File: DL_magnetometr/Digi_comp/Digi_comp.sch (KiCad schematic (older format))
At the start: 43 parts, among them J1 USB_B_Micro, U1 AP7331-WG-7, U2 74AHCT1G125, U3 JST-PHR-2, U4 AZ4558CM, U5 AZ4558CM, U6 AP7331-WG-7, U7 NUP2202, U8 HC-06

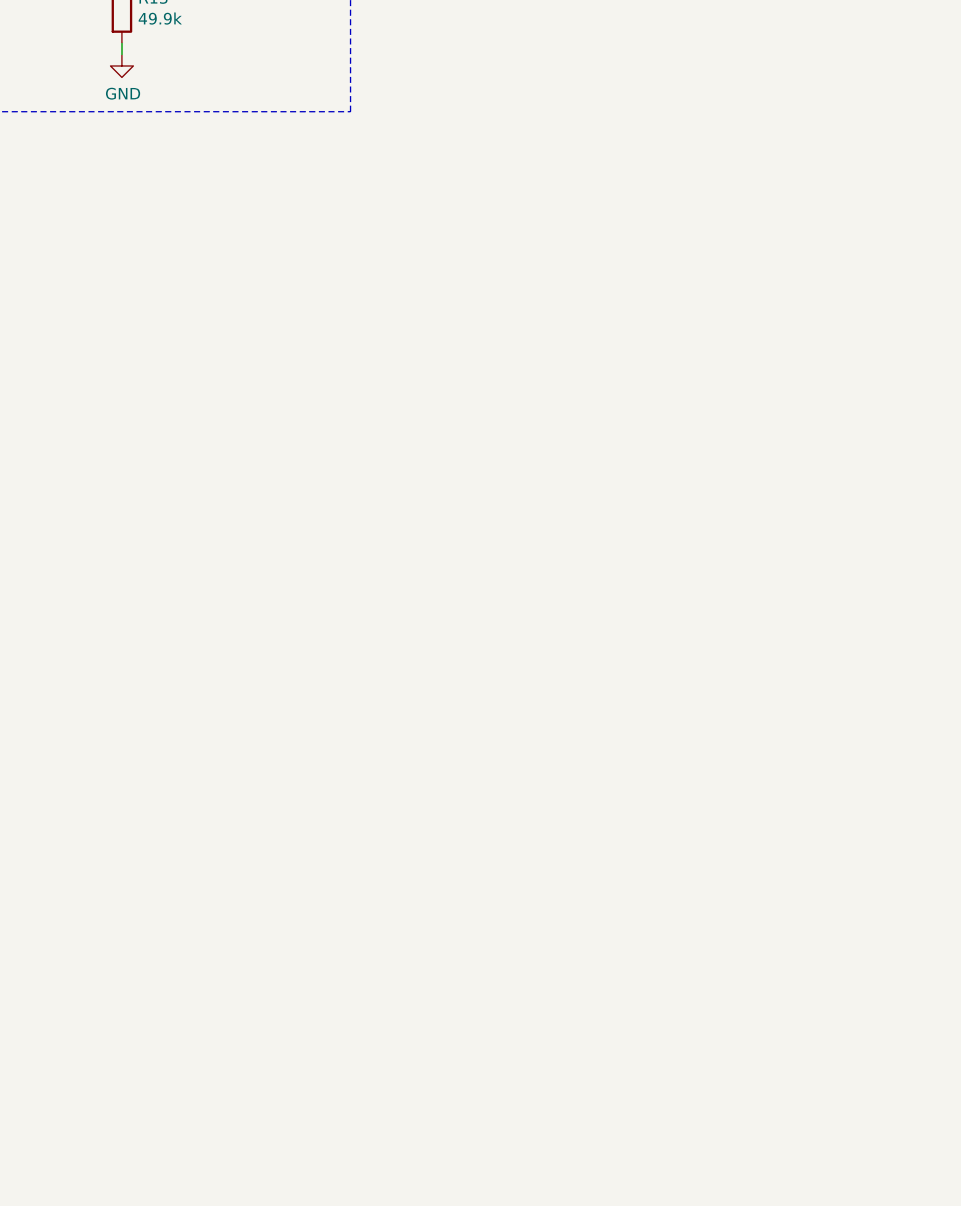
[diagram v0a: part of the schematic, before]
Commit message: Added AtMega328P
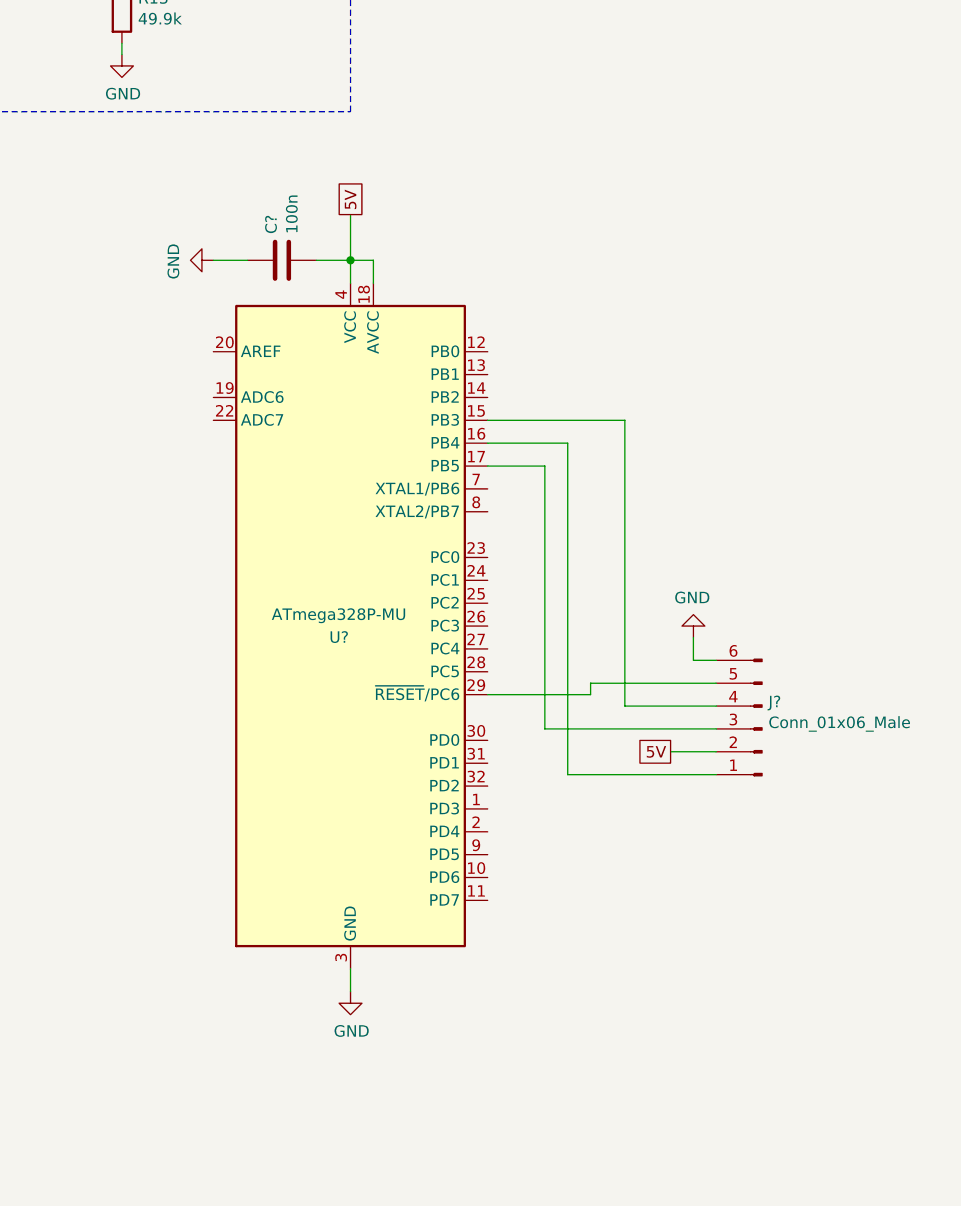
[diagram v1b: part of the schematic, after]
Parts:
- added C?: 100n, symbol Device:C
- added J?: Conn_01x06_Male, symbol Connector:Conn_01x06_Male
- added U?: ATmega328P-MU, Package_DFN_QFN:QFN-32-1EP_5x5mm_P0.5mm_EP3.1x3.1mm, symbol MCU_Microchip_ATmega:ATmega328P-MU
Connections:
- net 5V: now also C?.1, J?.2 (Pin_2), U?.18 (AVCC), U?.4 (VCC), U?.6 (VCC)
- net GND: now also C?.2, J?.6 (Pin_6), U?.21 (GND), U?.3 (GND), U?.33 (GND), U?.5 (GND)
- new net: J?.4 (Pin_4), U?.15 (PB3)
- new net: J?.1 (Pin_1), U?.16 (PB4)
- new net: J?.3 (Pin_3), U?.17 (PB5)
- new net: J?.5 (Pin_5), U?.29 (~RESET~/PC6)
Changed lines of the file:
@@
 Wire Notes Line
 	3350 2800 5750 2800
+$Comp
+L MCU_Microchip_ATmega:ATmega328P-MU U?
+U 1 1 5FFF77EE
+P 8750 5100
+F 0 "U?" H 8700 5050 50  0000 C CNN
+F 1 "ATmega328P-MU" H 8700 5150 50  0000 C CNN
+F 2 "Package_DFN_QFN:QFN-32-1EP_5x5mm_P0.5mm_EP3.1x3.1mm" H 8750 5100 50  0001 C CIN
+F 3 "http://ww1.microchip.com/downloads/en/DeviceDoc/ATmega328_P%20AVR%20MCU%20with%20picoPower%20Technology%20Data%20Sheet%2040001984A.pdf" H 8750 5100 50  0001 C CNN
+	1    8750 5100
+	1    0    0    -1
+$EndComp
+Wire Wire Line
+	8750 6700 8750 6600
+$Comp
+L power:GND #PWR?
+U 1 1 600084CF
+P 8750 6700
+F 0 "#PWR?" H 8750 6450 50  0001 C CNN
+F 1 "GND" H 8755 6527 50  0000 C CNN
+F 2 "" H 8750 6700 50  0001 C CNN
+F 3 "" H 8750 6700 50  0001 C CNN
+	1    8750 6700
+	1    0    0    -1
+$EndComp
+Text GLabel 8750 3300 1    50   UnSpc ~ 0
+5V
+$Comp
+L Device:C C?
+U 1 1 6001938B
+P 8450 3500
+F 0 "C?" H 8335 3454 50  0000 R CNN
+F 1 "100n" H 8335 3545 50  0000 R CNN
+F 2 "" H 8488 3350 50  0001 C CNN
+F 3 "~" H 8450 3500 50  0001 C CNN
+	1    8450 3500
+	0    1    1    0
+$EndComp
+$Comp
+L power:GND #PWR?
+U 1 1 6001A392
+P 8150 3500
+F 0 "#PWR?" H 8150 3250 50  0001 C CNN
+F 1 "GND" H 8155 3327 50  0000 C CNN
+F 2 "" H 8150 3500 50  0001 C CNN
+F 3 "" H 8150 3500 50  0001 C CNN
+	1    8150 3500
+	0    1    1    0
+$EndComp
+Wire Wire Line
+	8750 3300 8750 3500
+Connection ~ 8750 3500
+Wire Wire Line
+	8750 3500 8750 3600
+Wire Wire Line
+	8850 3600 8850 3500
+Wire Wire Line
+	8850 3500 8750 3500
+Wire Wire Line
+	8600 3500 8750 3500
+Wire Wire Line
+	8300 3500 8150 3500
+$Comp
+L Connector:Conn_01x06_Male J?
+U 1 1 60070624
+P 10550 5550
+F 0 "J?" H 10522 5432 50  0000 R CNN
+F 1 "Conn_01x06_Male" H 10522 5523 50  0000 R CNN
+F 2 "" H 10550 5550 50  0001 C CNN
+F 3 "~" H 10550 5550 50  0001 C CNN
+	1    10550 5550
+	-1   0    0    1
+$EndComp
+$Comp
+L power:GND #PWR?
+U 1 1 60072062
+P 10250 5150
+F 0 "#PWR?" H 10250 4900 50  0001 C CNN
+F 1 "GND" H 10255 4977 50  0000 C CNN
+F 2 "" H 10250 5150 50  0001 C CNN
+F 3 "" H 10250 5150 50  0001 C CNN
+	1    10250 5150
+	-1   0    0    1
+$EndComp
+Wire Wire Line
+	10350 5250 10250 5250
+Wire Wire Line
+	10250 5250 10250 5150
+Wire Wire Line
+	10350 5350 9800 5350
+Wire Wire Line
+	9800 5350 9800 5400
+Wire Wire Line
+	9800 5400 9350 5400
+Text GLabel 10150 5650 0    50   UnSpc ~ 0
+5V
+Wire Wire Line
+	10350 5650 10150 5650
+Wire Wire Line
+	10350 5750 9700 5750
+Wire Wire Line
+	9700 5750 9700 4300
+Wire Wire Line
+	9700 4300 9350 4300
+Wire Wire Line
+	10350 5450 9950 5450
+Wire Wire Line
+	9950 5450 9950 4200
+Wire Wire Line
+	9950 4200 9350 4200
+Wire Wire Line
+	10350 5550 9600 5550
+Wire Wire Line
+	9600 5550 9600 4400
+Wire Wire Line
+	9600 4400 9350 4400
 $EndSCHEMATC
